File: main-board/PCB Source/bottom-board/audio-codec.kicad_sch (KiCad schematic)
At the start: 36 parts, among them U13 AP2120N-3.3, U3 CS4265, X1 24.576MHz

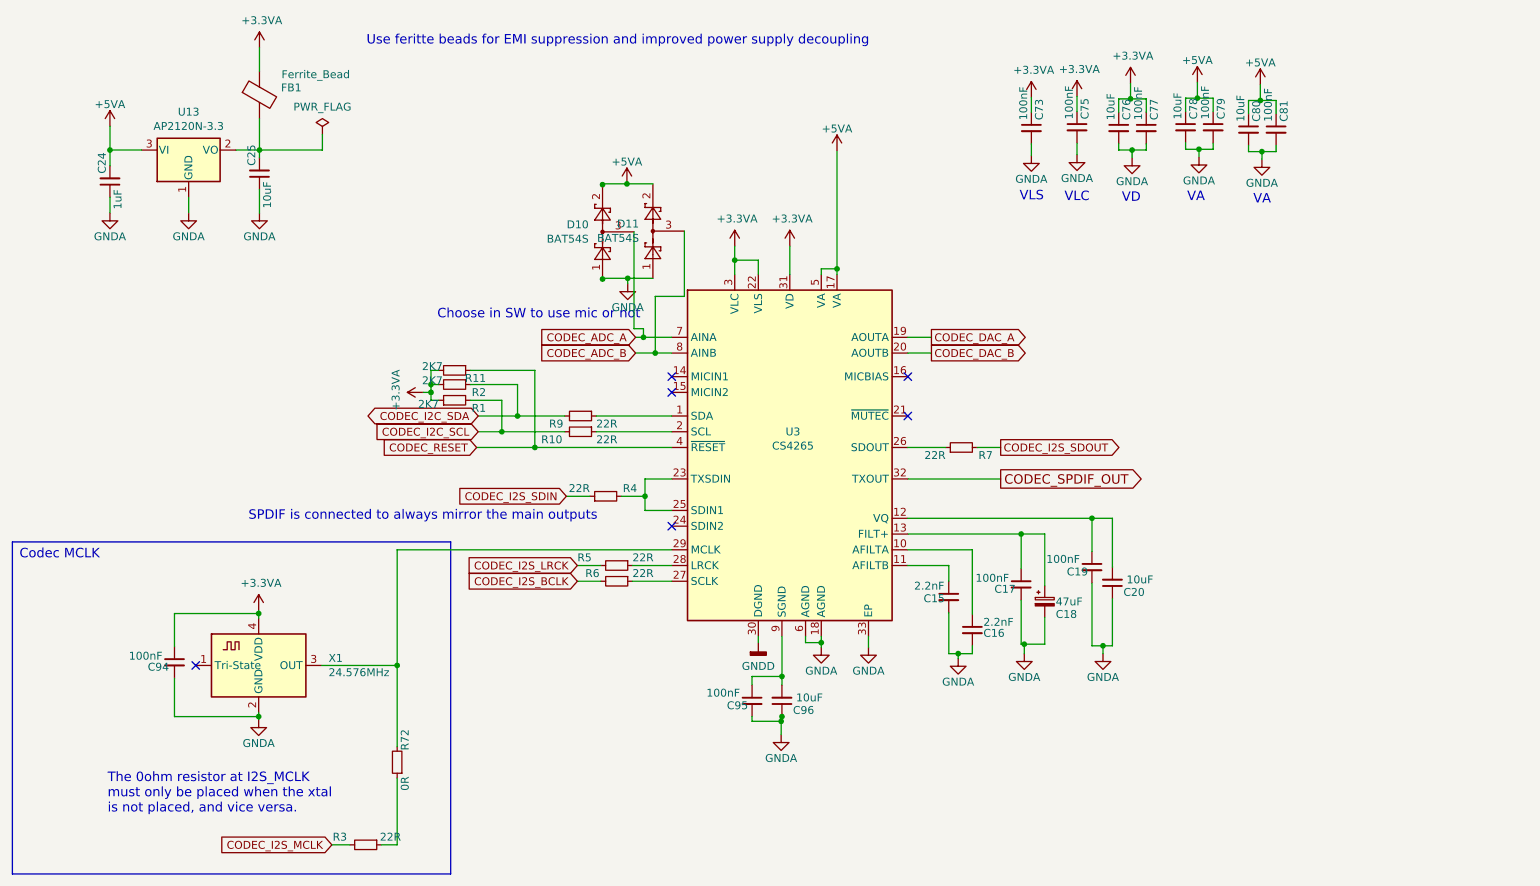
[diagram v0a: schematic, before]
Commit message: mainboard: add bias buffer, update MPNs, clean schematic
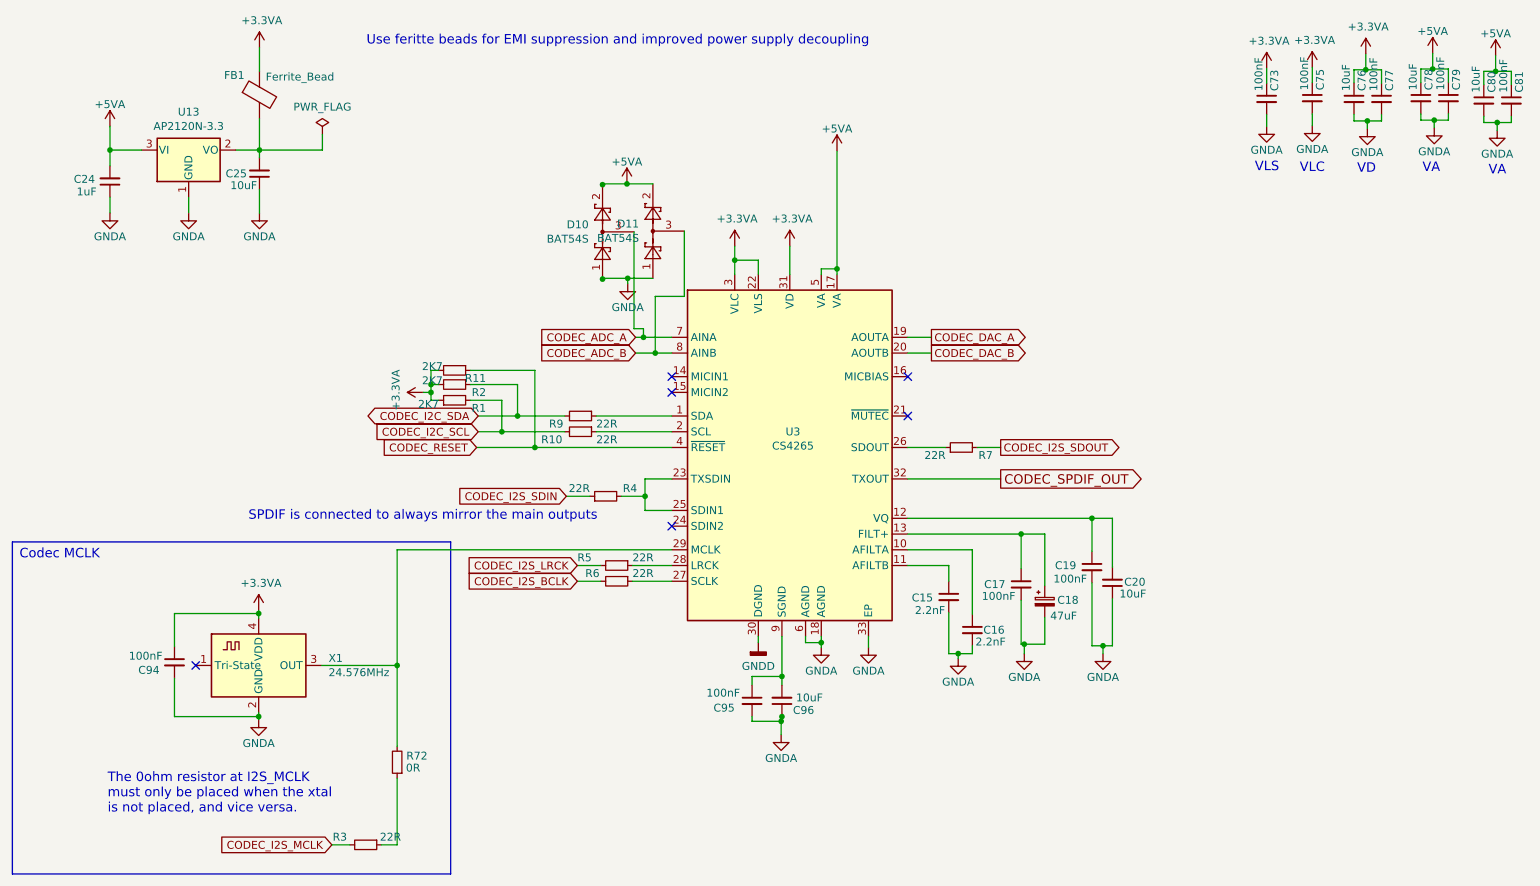
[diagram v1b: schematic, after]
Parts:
- C94: MPN GCM188R71C104KA37D -> DO NOT PLACE
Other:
- note removed: "Choose in SW to use mic or not"
- moved on the sheet: C73, C75, C76, C77, C78, C79, C80, C81
